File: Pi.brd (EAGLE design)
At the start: 160 x 100 mm, 11 parts, among them X1 RASPI_GPIO_B+#_BOX, X2 HDD, 5V 700mA, X3 MAC64L

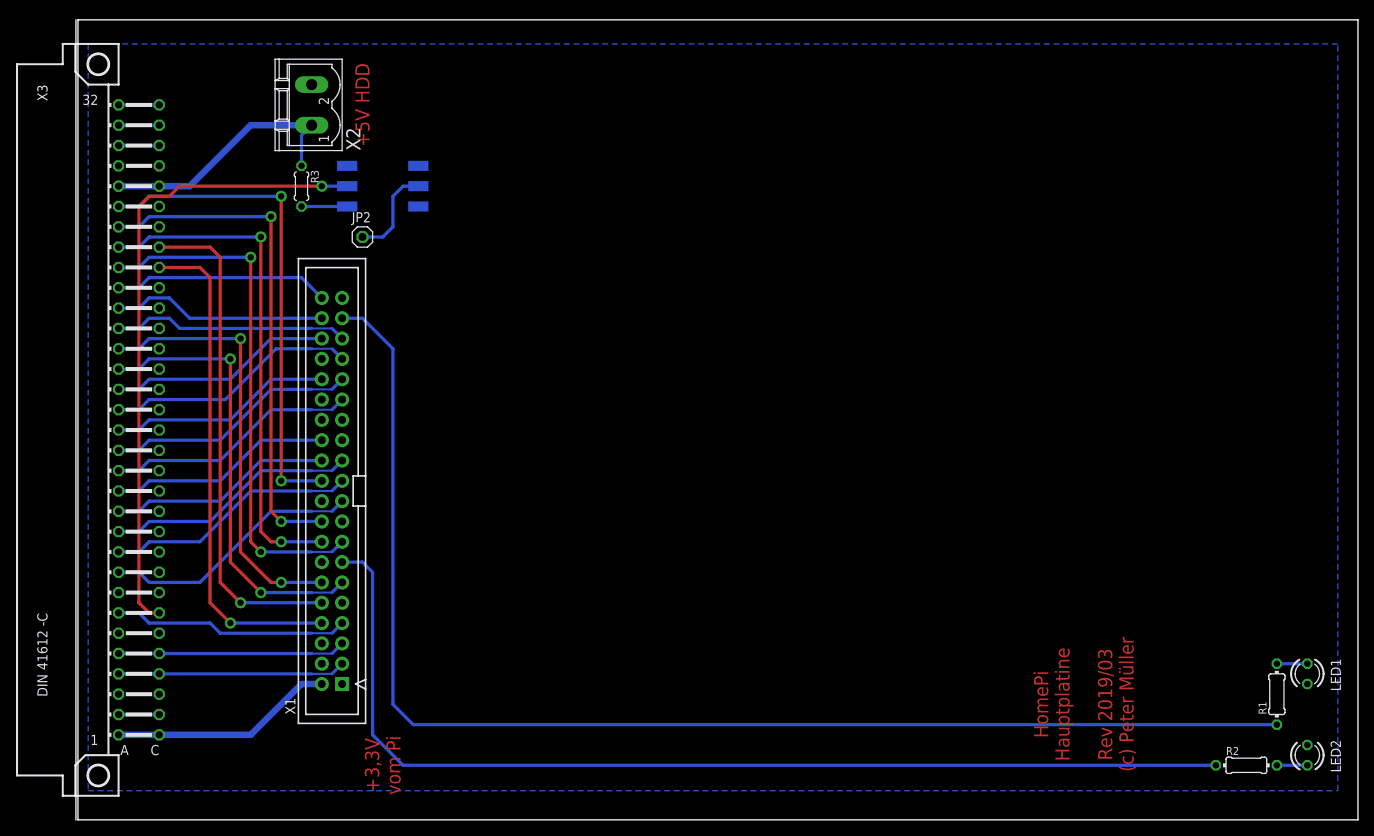
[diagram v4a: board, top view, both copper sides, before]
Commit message: 1-Wire Sensor auf Raspi-Platine
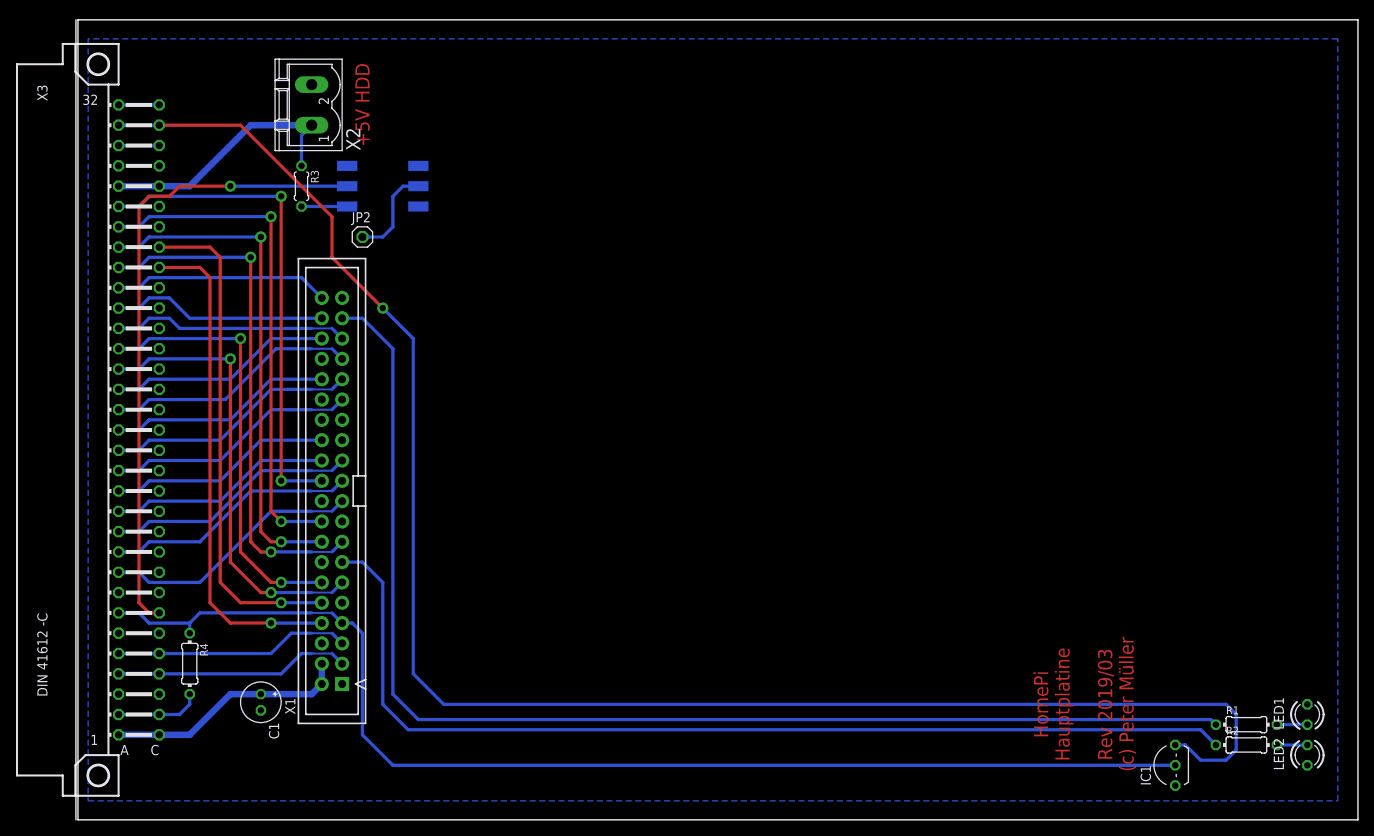
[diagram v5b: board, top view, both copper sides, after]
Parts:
- added C1: 47µF 16V Low-ESR, rcl:E2-5
- added IC1: DS18B20, 1wire:TO92-
- added R4: 4k7, rcl:0204/7
- moved R1 5.39 mm to (146.1, 11.4), turned to 0 degrees
- moved LED1 5.08 mm to (153.7, 12.7), turned to 90 degrees
- moved R2 2.54 mm to (146.1, 8.89)
- turned LED2 to 270 degrees
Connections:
- removed net 5V0B: X1.4
- net +3,3V: now also R4.2
- net +5V_EXT: now also IC1.3
- net +5V_INT: now also C1.+, X1.4
- net 1WIRE: now also IC1.2, R4.1
- net GND: now also C1.-, IC1.1
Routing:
- net +5V_EXT: track 5.08 -> 211.1 mm, vias 0 -> 1
- net 1WIRE: track 29.5 -> 149.7 mm
- net GPIO.26: track 163.9 -> 155.6 mm
- net +3,3V: track 5.08 -> 10.7 mm
- net GPIO.27: track 131.6 -> 127.6 mm
- net +5V_INT: track 28.0 -> 30.6 mm
- net I2C_SDA: track 28.5 -> 29.5 mm
- net I2C_SCL: track 28.5 -> 29.5 mm
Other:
- board text removed: "+3,3V vom Pi"

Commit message: Diverse Anpassungen
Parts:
- X1: value RASPI_GPIO_B+#_BOX -> RASPI_GPIO_B+#_PIN; device raspberrypi_bastelstube_v13:RASPI_GPIO_B+_BOX -> raspberrypi_bastelstube_v13:RASPI_GPIO_B+_PIN
- moved JP2 105.6 mm to (139.7, 90.2)
- moved C1 91.2 mm to (74.9, 89.2)
- moved X1 89.1 mm to (106.7, 88.9), turned to 0 degrees
- moved RPI1 18.4 mm to (74.3, 29.8)
- moved R3 13.7 mm to (40.6, 83.8)
- moved OK1 12.5 mm to (49.5, 83.8)
- moved LED1 2.54 mm to (153.7, 15.2)
- moved R1 2.54 mm to (146.1, 14.0)
- moved LED2 2.54 mm to (153.7, 10.2)
- moved R2 2.54 mm to (146.1, 11.4)
- moved IC1 1.27 mm to (138.4, 6.35), turned to 270 degrees
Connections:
- net RS485_A renamed CANL
- net RS495_B renamed CANH
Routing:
- net SPI_MISO: track 31.6 -> 163.9 mm, vias 0 -> 2
- net SPI_CE1: track 28.0 -> 158.5 mm, vias 0 -> 2
- net SPI_CE0: track 28.0 -> 158.5 mm, vias 0 -> 2
- net SPI_MOSI: track 32.7 -> 161.4 mm, vias 0 -> 2
- net GPIO.16: track 28.0 -> 156.0 mm, vias 0 -> 2
- net GPIO.12: track 28.0 -> 156.0 mm, vias 0 -> 2
- net +5V_INT: track 30.6 -> 158.5 mm
- net SPI_SCLK: track 31.6 -> 157.4 mm, vias 0 -> 2
- net GPIO.06: track 31.6 -> 156.7 mm, vias 0 -> 2
- net GPIO.05: track 31.6 -> 156.7 mm, vias 0 -> 2
- net GPIO.21: track 27.0 -> 150.9 mm, vias 0 -> 2
- net GPIO.13: track 31.6 -> 154.2 mm, vias 0 -> 2
- net GPIO.20: track 27.0 -> 148.4 mm, vias 0 -> 2
- net I2C_SDA: track 29.5 -> 149.9 mm, vias 0 -> 2
- net I2C_SCL: track 29.5 -> 149.9 mm, vias 0 -> 2
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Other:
- board text added: "Pi Reset"

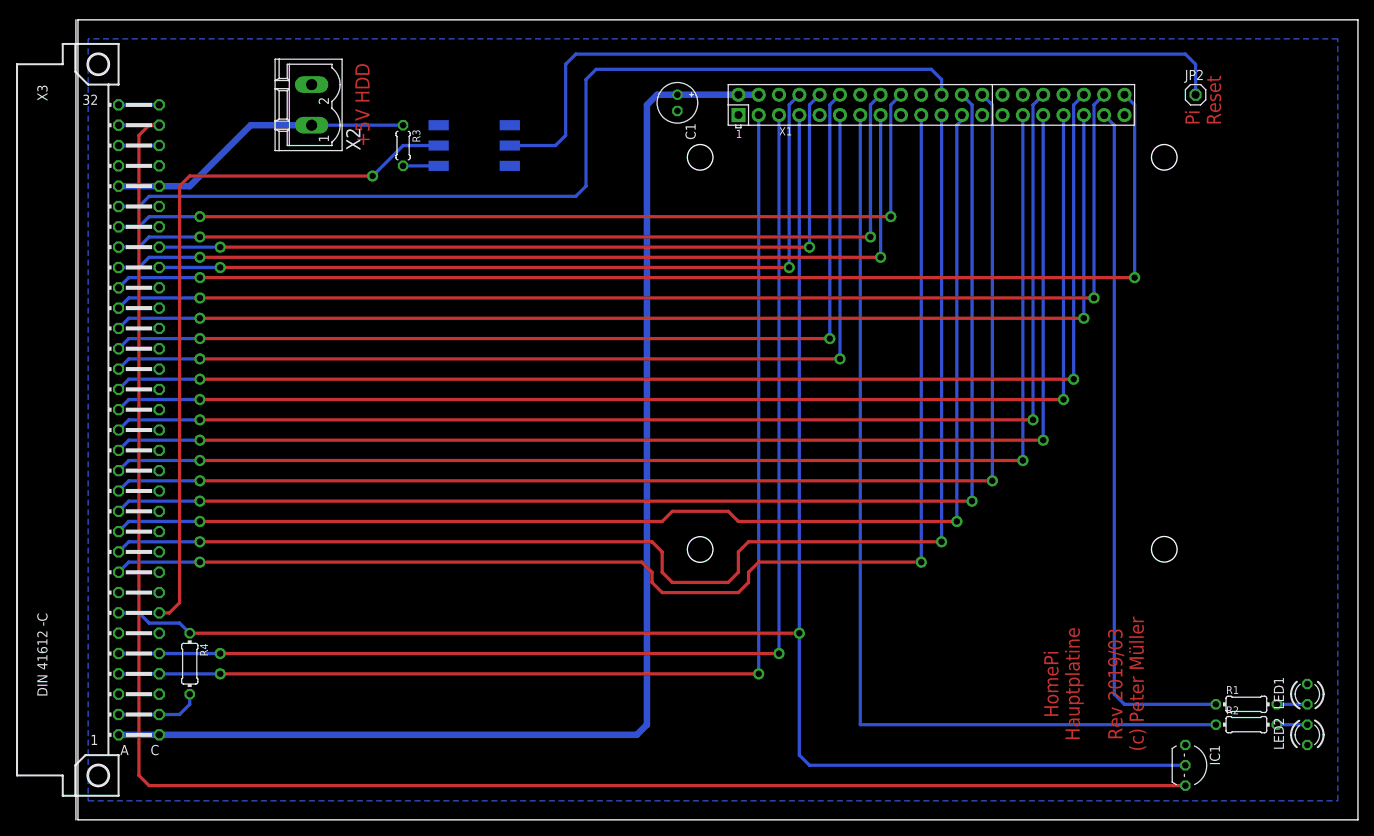
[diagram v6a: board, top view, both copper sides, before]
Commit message: Pi, CanBus, Stromversorgung, Steckverbinder angepasst
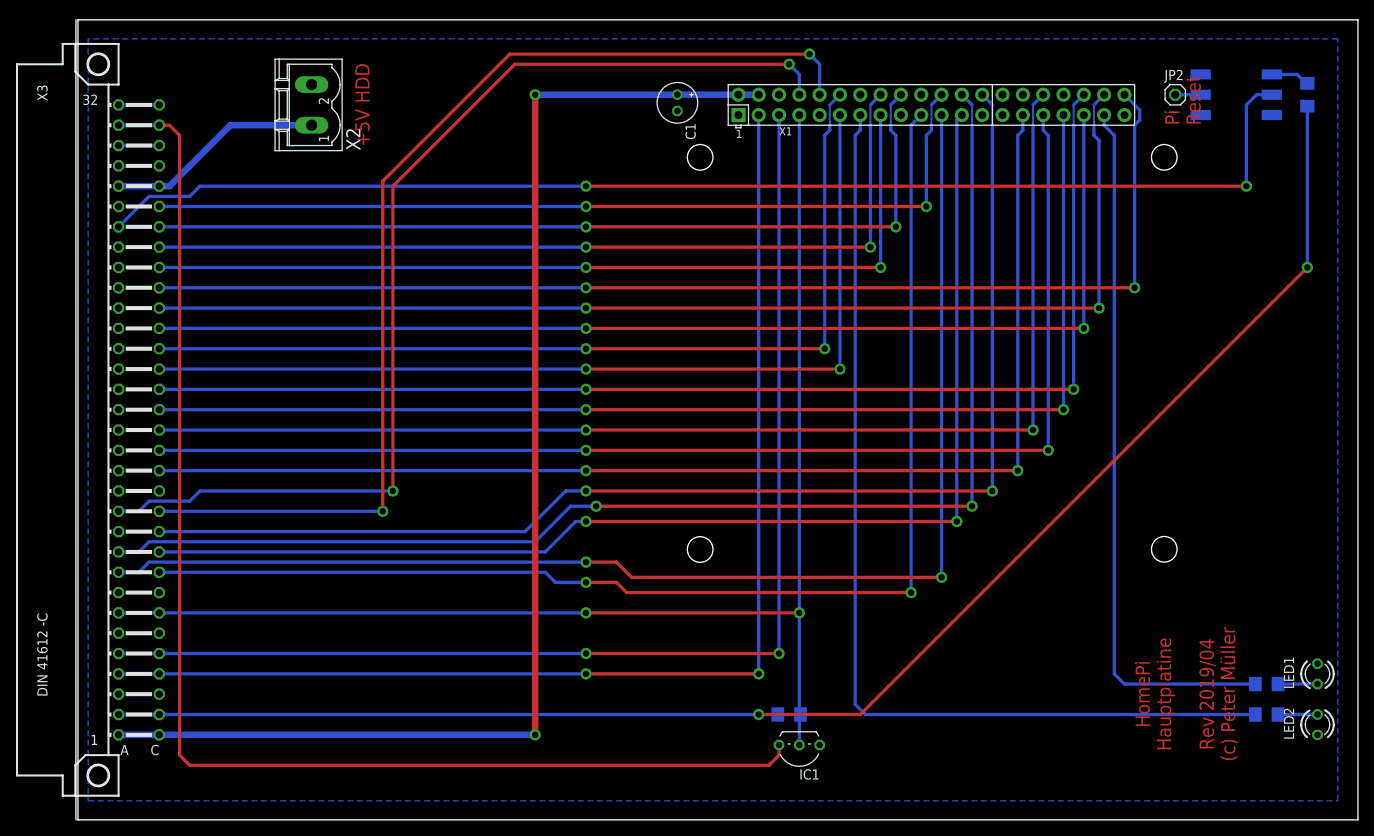
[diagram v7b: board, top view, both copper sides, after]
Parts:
- JP2: value (none) -> PI Reset
- R1, R2, R4: device rcl:0204/7 -> rcl:R1206
- R3: device rcl:0204/5 -> rcl:R1206
- moved R3 113.2 mm to (153.7, 90.2), flipped to the bottom, turned to 90 degrees
- moved OK1 95.5 mm to (144.8, 90.2), turned to 270 degrees
- moved R4 75.2 mm to (88.9, 12.7), flipped to the bottom, turned to 0 degrees
- moved IC1 48.3 mm to (90.2, 8.89), turned to 180 degrees
- moved R1 3.59 mm to (148.6, 16.5), flipped to the bottom, turned to 180 degrees
- moved LED1 2.84 mm to (154.9, 17.8)
- moved R2 2.84 mm to (148.6, 12.7), flipped to the bottom, turned to 180 degrees
- moved JP2 2.54 mm to (137.2, 90.2)
- moved LED2 1.80 mm to (154.9, 11.4)
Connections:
- removed net CANH: X3.C27
- removed net CANL: X3.C26
- removed net RXD: X1.10, X3.C25
- removed net TXD: X1.8, X3.C24
- new net PI_RXD: X1.10, X3.C12
- new net PI_TXD: X1.8, X3.A12
- net !PI_RESET: now also X3.A26; no longer X3.C7
- net +3,3V: now also R3.1
- net +5V_INT2: no longer R3.1
- net 1WIRE: now also X3.C7
- net GPIO.05: now also X3.C14; no longer X3.A14
- net GPIO.06: now also X3.C15; no longer X3.A15
- net GPIO.12: now also X3.C16; no longer X3.A16
- net GPIO.13: now also X3.C17; no longer X3.A17
- net GPIO.16: now also X3.C18; no longer X3.A18
- net GPIO.17: now also X3.C19; no longer X3.A19
- net GPIO.18: now also X3.C20; no longer X3.A20
- net GPIO.19: now also X3.C21; no longer X3.A21
- net GPIO.20: now also X3.C22; no longer X3.A22
- net GPIO.21: now also X3.C23; no longer X3.A23
- net GPIO.22: now also X3.C24; no longer X3.A24
- net GPIO.23: now also X3.C25; no longer X3.A25
- net GPIO.24: now also X3.C26; no longer X3.A26
- net GPIO.25: now also X3.C27; no longer X3.A27
- net SPI_CE0: now also X3.A10; no longer X3.A12
- net SPI_CE1: now also X3.C11; no longer X3.A13
- net SPI_MISO: now also X3.A9; no longer X3.A10
- net SPI_MOSI: now also X3.C9; no longer X3.A9
- net SPI_SCLK: now also X3.C10; no longer X3.A11
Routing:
- net +3,3V: track 10.7 -> 194.3 mm, vias 0 -> 2
- net PI_RXD: track 0.00 -> 134.7 mm, vias 0 -> 2
- net PI_TXD: track 0.00 -> 133.6 mm, vias 0 -> 2
- net TXD: track 100.9 -> 0.00 mm, vias 2 -> 0
- net RXD: track 100.9 -> 0.00 mm, vias 2 -> 0
- net N$3: track 100.0 -> 3.18 mm
- net !PI_RESET: track 89.6 -> 156.9 mm, vias 1 -> 2
- net +5V_EXT: track 219.5 -> 162.9 mm
- net 1WIRE: track 214.9 -> 164.0 mm, vias 1 -> 2
- net +5V_INT2: track 38.7 -> 27.3 mm
- net GPIO.25: track 120.2 -> 110.6 mm, vias 0 -> 2
- net SPI_MOSI: track 161.4 -> 155.2 mm
- net SPI_SCLK: track 157.4 -> 152.3 mm
- net GPIO.18: track 120.4 -> 115.7 mm
- net GPIO.05: track 156.7 -> 152.0 mm
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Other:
- board text added: "HomePi Hauptplatine Rev 2019/04 (c) Peter Müller"
- board text removed: "HomePi Hauptplatine Rev 2019/03 (c) Peter Müller"

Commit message: Platinen angepasst, Backplane
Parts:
- moved X2 76.7 mm to (38.1, 12.7)
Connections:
- net +5V_INT: now also X2.1; no longer C1.+, X1.2, X1.4
- net +5V_INT2: now also C1.+, X1.2, X1.4; no longer X2.1
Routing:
- net +5V_INT: track 160.0 -> 33.0 mm, vias 2 -> 0
- net +5V_INT2: track 27.3 -> 84.7 mm
- net +5V_EXT: track 162.9 -> 166.2 mm, vias 0 -> 2
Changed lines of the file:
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@@
 Rev 2019/04
 (c) Peter Müller</text>
-<text x="35.56" y="88.9" size="1.778" layer="1" font="vector" ratio="15" rot="R90" align="center">+5V HDD</text>
+<text x="44.45" y="12.7" size="1.778" layer="1" font="vector" ratio="15" rot="R90" align="center">+5V HDD</text>
 <dimension x1="5" y1="50" x2="0" y2="0" x3="-6.35" y3="25" textsize="1.778" layer="47" dtype="vertical" visible="yes"/>
 <dimension x1="0" y1="100" x2="2.54" y2="0" x3="-12.7" y3="50" textsize="1.778" layer="47" dtype="vertical" visible="yes"/>
@@
 <attribute name="VALUE" x="153.289" y="9.525" size="1.27" layer="27" ratio="10" rot="R270"/>
 </element>
-<element name="X2" library="con-phoenix-508" package="MSTBV2" value="HDD, 5V 700mA" x="29.21" y="88.9" rot="R90">
-<attribute name="OC_NEWARK" value="69R9845" x="29.21" y="88.9" size="1.778" layer="27" rot="R90" display="off"/>
-<attribute name="MF" value="" x="29.21" y="88.9" size="1.778" layer="27" rot="R90" display="off"/>
-<attribute name="MPN" value="MSTBV 2,5/2-GF-5.08" x="29.21" y="88.9" size="1.778" layer="27" rot="R90" display="off"/>
-<attribute name="OC_FARNELL" value="1792792" x="29.21" y="88.9" size="1.778" layer="27" rot="R90" display="off"/>
+<element name="X2" library="con-phoenix-508" package="MSTBV2" value="HDD, 5V 700mA" x="38.1" y="12.7" rot="R90">
+<attribute name="OC_NEWARK" value="69R9845" x="38.1" y="12.7" size="1.778" layer="27" rot="R90" display="off"/>
+<attribute name="MF" value="" x="38.1" y="12.7" size="1.778" layer="27" rot="R90" display="off"/>
+<attribute name="MPN" value="MSTBV 2,5/2-GF-5.08" x="38.1" y="12.7" size="1.778" layer="27" rot="R90" display="off"/>
+<attribute name="OC_FARNELL" value="1792792" x="38.1" y="12.7" size="1.778" layer="27" rot="R90" display="off"/>
 </element>
 <element name="X3" library="con-vg" package="MAC64L" value="MAC64L" x="2.54" y="49.53" rot="R180"/>
@@
 </signal>
 <signal name="+5V_INT2">
-<contactref element="X2" pad="1"/>
-<wire x1="11.43" y1="78.74" x2="19.05" y2="86.36" width="0.8128" layer="16"/>
-<wire x1="19.05" y1="86.36" x2="29.21" y2="86.36" width="0.8128" layer="16"/>
 <contactref element="X3" pad="A28"/>
 <contactref element="X3" pad="C28"/>
 <wire x1="10.16" y1="78.74" x2="5.08" y2="78.74" width="0.8128" layer="16"/>
-<wire x1="11.43" y1="78.74" x2="10.16" y2="78.74" width="0.8128" layer="16"/>
+<contactref element="C1" pad="+"/>
+<contactref element="X1" pad="4"/>
+<contactref element="X1" pad="2"/>
+<wire x1="10.16" y1="78.74" x2="11.43" y2="78.74" width="0.8128" layer="16"/>
+<wire x1="11.43" y1="78.74" x2="22.86" y2="90.17" width="0.8128" layer="16"/>
+<wire x1="22.86" y1="90.17" x2="74.924" y2="90.17" width="0.8128" layer="16"/>
+<wire x1="74.924" y1="90.17" x2="74.93" y2="90.176" width="0.8128" layer="16"/>
+<wire x1="85.09" y1="90.17" x2="82.55" y2="90.17" width="0.8128" layer="16"/>
+<wire x1="82.55" y1="90.17" x2="74.936" y2="90.17" width="0.8128" layer="16"/>
+<wire x1="74.936" y1="90.17" x2="74.93" y2="90.176" width="0.8128" layer="16"/>
 </signal>
 <signal name="+5V_INT">
-<contactref element="X1" pad="2"/>
 <contactref element="X3" pad="A1"/>
 <contactref element="X3" pad="C1"/>
 <wire x1="10.16" y1="10.16" x2="5.08" y2="10.16" width="0.8128" layer="16"/>
-<contactref element="C1" pad="+"/>
-<contactref element="X1" pad="4"/>
-<wire x1="85.09" y1="90.17" x2="82.55" y2="90.17" width="0.8128" layer="16"/>
-<wire x1="82.55" y1="90.17" x2="82.544" y2="90.176" width="0.8128" layer="16"/>
-<wire x1="82.544" y1="90.176" x2="74.93" y2="90.176" width="0.8128" layer="16"/>
-<wire x1="10.16" y1="10.16" x2="57.15" y2="10.16" width="0.8128" layer="16"/>
-<via x="57.15" y="10.16" extent="1-16" drill="0.8" diameter="1.4224"/>
-<wire x1="57.15" y1="10.16" x2="57.15" y2="90.17" width="0.8128" layer="1"/>
-<via x="57.15" y="90.17" extent="1-16" drill="0.8" diameter="1.4224"/>
-<wire x1="57.15" y1="90.17" x2="74.924" y2="90.17" width="0.8128" layer="16"/>
-<wire x1="74.924" y1="90.17" x2="74.93" y2="90.176" width="0.8128" layer="16"/>
+<contactref element="X2" pad="1"/>
+<wire x1="10.16" y1="10.16" x2="38.1" y2="10.16" width="0.8128" layer="16"/>
 </signal>
 <signal name="GND_EXT">
@@
 <wire x1="10.16" y1="86.36" x2="5.08" y2="86.36" width="0.4064" layer="16"/>
 <contactref element="IC1" pad="3"/>
-<wire x1="10.16" y1="86.36" x2="11.43" y2="86.36" width="0.4064" layer="1"/>
-<wire x1="11.43" y1="86.36" x2="12.7" y2="85.09" width="0.4064" layer="1"/>
-<wire x1="12.7" y1="85.09" x2="12.7" y2="7.62" width="0.4064" layer="1"/>
-<wire x1="13.97" y1="6.35" x2="86.36" y2="6.35" width="0.4064" layer="1"/>
-<wire x1="86.36" y1="6.35" x2="87.63" y2="7.62" width="0.4064" layer="1"/>
-<wire x1="87.63" y1="7.62" x2="87.63" y2="8.89" width="0.4064" layer="1"/>
-<wire x1="13.97" y1="6.35" x2="12.7" y2="7.62" width="0.4064" layer="1"/>
+<wire x1="87.63" y1="8.89" x2="87.63" y2="7.62" width="0.4064" layer="16"/>
+<wire x1="87.63" y1="7.62" x2="85.09" y2="5.08" width="0.4064" layer="16"/>
+<wire x1="85.09" y1="5.08" x2="13.97" y2="5.08" width="0.4064" layer="16"/>
+<via x="13.97" y="5.08" extent="1-16" drill="0.8" diameter="1.4224"/>
+<wire x1="13.97" y1="5.08" x2="13.97" y2="86.36" width="0.4064" layer="1"/>
+<via x="13.97" y="86.36" extent="1-16" drill="0.8" diameter="1.4224"/>
+<wire x1="13.97" y1="86.36" x2="10.16" y2="86.36" width="0.4064" layer="16"/>
 </signal>
 <signal name="+24V">
